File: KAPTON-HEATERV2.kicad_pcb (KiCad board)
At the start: 2 copper layers, 90 x 90 mm, 32 parts, among them J1 XT60PW-M, J2 XT60PW-M, J3 1985276, J4 1985218, J5 10090926-P154XLF, K1 1-1393210-8, Q1 AO3400A, U1 TC4427ACOA, U2 INA181

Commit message: iteration 1.2
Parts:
- removed the R5 at (95.4, 57.0)
- added D3: SMCJ30CA, PCM_JLCPCB:D_SMC, F.Cu at (105.0, 127.5)
- added R8: R27, Resistor_SMD:R_1206_3216Metric, F.Cu at (99.2, 121.2)
- C4: value C19nf -> C4.7nf
- MOSFET1: value SIR462DP-T1-GE3 -> SIR626ADP
- R6: value R10 -> R5
- moved C1 103.9 mm to (58.1, 81.1), turned to 180 degrees
- moved C3 90.3 mm to (76.0, 115.6)
- moved C5 89.2 mm to (76.0, 117.8)
- moved R1 67.4 mm to (62.4, 92.6), turned to 0 degrees
- moved C4 62.6 mm to (99.2, 125.6)
- moved R2 61.8 mm to (63.7, 85.8)
- moved C6 59.8 mm to (72.4, 106.2), turned to 180 degrees
- moved R6 58.4 mm to (53.1, 86.6)
- moved U1 57.7 mm to (58.1, 85.1)
- moved MOSFET1 56.4 mm to (115.0, 128.1)
- moved J4 53.0 mm to (81.0, 66.3), turned to 180 degrees
- moved C2 49.9 mm to (58.1, 78.7), turned to 180 degrees
- moved J5 46.2 mm to (107.7, 70.5), turned to 180 degrees
- moved R3 38.9 mm to (61.8, 81.0)
- moved D1 33.9 mm to (76.0, 96.0), turned to -90 degrees
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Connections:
- net /24VIN renamed Net-(J2-Pin_2)
- D2 pad 3: (no net) -> /24V
- F1 pad 2: unconnected-(F1-Pad2) -> Net-(F1-Pad2)
- J1 pad S1: (no net) -> GND
- J1 pad S2: (no net) -> GND
- K1 pad 3: unconnected-(K1-Pad3) -> Net-(F1-Pad2)
- MOSFET1 pad 4: Net-(C4-Pad1) -> Net-(MOSFET1-Pad4)
- R6 pad 1: Net-(C4-Pad1) -> Net-(MOSFET1-Pad4)
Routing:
- net Current Vout: track 0.00 -> 117.8 mm
- net Net-(MOSFET1-Pad4): track 0.00 -> 110.8 mm
- net HEATER OUT: track 0.00 -> 87.3 mm
- net GND: track 15.8 -> 84.6 mm, vias 2 -> 0
- net TH8: track 94.5 -> 34.6 mm, vias 4 -> 0
- net TH9: track 87.7 -> 32.7 mm, vias 4 -> 0
- net Net-(Q1-Pad1): track 60.5 -> 6.11 mm, vias 4 -> 0
- net TH1: track 95.2 -> 48.9 mm, vias 1 -> 0
- net TH2: track 92.6 -> 47.9 mm, vias 1 -> 0
- net TH5: track 74.9 -> 35.0 mm, vias 3 -> 0
- net TH7: track 79.0 -> 40.6 mm, vias 2 -> 0
- net TH4: track 82.0 -> 45.5 mm, vias 1 -> 0
- net TH3: track 82.6 -> 46.7 mm, vias 1 -> 0
- net PWM: track 7.70 -> 39.2 mm
- net Net-(D1-A): track 48.7 -> 24.2 mm, vias 2 -> 1
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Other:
- board size 90 x 90 mm -> 90 x 76 mm
- board text added: "BRANDON M ASLAN L ZHIHAN C HEATER CONTROL QRET 2025"
- board text added: "IOUT"
- board text added: "PWM"
- board text added: "RELAY"
- board text removed: "BRANDON M ASLAN L QRET 2025"
- board text removed: "PWM IN (3.3V)"
- board text removed: "RELAY (3.3V)"

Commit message: trace fix
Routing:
- net /24V: track 53.0 -> 58.1 mm
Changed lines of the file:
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@@
+	)
+	(segment
+		(start 82.35 117.46)
+		(end 82.35 122.54)
+		(width 4)
+		(layer "F.Cu")
+		(net 18)
 	)
 	(segment
@@
 	)
 	(segment
-		(start 75 130)
+		(start 112.7 131)
+		(end 112.8 130.9)
+		(width 4)
+		(layer "F.Cu")
+		(net 20)
+	)
+	(segment
+		(start 71.4 114.975)
 		(end 71.4 126.4)
+		(width 4)
+		(layer "F.Cu")
+		(net 20)
+	)
+	(segment
+		(start 71.4 126.4)
+		(end 76 131)
 		(width 4)
 		(layer "F.Cu")
@@
 	)
 	(segment
+		(start 76 131)
+		(end 104.9 131)
+		(width 4)
+		(layer "F.Cu")
+		(net 20)
+	)
+	(segment
 		(start 91.5 128.5)
 		(end 90 130)
@@
 	)
 	(segment
+		(start 105 130.9)
+		(end 105.1 131)
+		(width 4)
+		(layer "F.Cu")
+		(net 20)
+	)
+	(segment
 		(start 116.805 130.9)
 		(end 116.905 131)
@@
 	)
 	(segment
-		(start 90 130)
-		(end 75 130)
-		(width 4)
-		(layer "F.Cu")
-		(net 20)
-	)
-	(segment
 		(start 112.8 130.9)
 		(end 116.805 130.9)
@@
 	)
 	(segment
-		(start 90 130)
-		(end 90.9 130.9)
+		(start 105.1 131)
+		(end 112.7 131)
 		(width 4)
 		(layer "F.Cu")
@@
 	)
 	(segment
-		(start 71.4 126.4)
-		(end 71.4 114.975)
-		(width 4)
-		(layer "F.Cu")
-		(net 20)
-	)
-	(segment
 		(start 114.998 128.702)
 		(end 112.8 130.9)
@@
 	)
 	(segment
+		(start 104.9 131)
+		(end 105 130.9)
+		(width 4)
+		(layer "F.Cu")
+		(net 20)
+	)
+	(segment
 		(start 91.7625 119.7375)
 		(end 91.5 120)
@@
 	)
 	(segment
-		(start 90.9 130.9)
-		(end 105 130.9)
-		(width 4)
-		(layer "F.Cu")
-		(net 20)
-	)
-	(segment
 		(start 114.998 129.093)
 		(end 116.905 131)
@@
 		(start 91.5 120)
 		(end 91.5 128.5)
-		(width 4)
-		(layer "F.Cu")
-		(net 20)
-	)
-	(segment
-		(start 105 130.9)
-		(end 112.8 130.9)
 		(width 4)
 		(layer "F.Cu")
@@
 		(min_thickness 0.25)
 		(filled_areas_thickness no)
-		(fill
+		(fill yes
 			(thermal_gap 0.5)
 			(thermal_bridge_width 0.5)

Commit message: fixed DRC issues and made some traces pretty
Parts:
- turned C4 to -90 degrees
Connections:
- J2 pad S1: (no net) -> GND
- J2 pad S2: (no net) -> GND
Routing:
- net GND: track 84.6 -> 112.4 mm
- net TH9: track 32.7 -> 52.3 mm
- net TH4: track 45.5 -> 40.1 mm
- net TH1: track 48.9 -> 53.1 mm
- net TH6: track 98.3 -> 94.9 mm
- net Current Vout: track 117.8 -> 119.7 mm
- net TH7: track 40.6 -> 38.9 mm
- net TH8: track 34.6 -> 35.2 mm
- net TH3: track 46.7 -> 47.3 mm
- net TH2: track 47.9 -> 48.4 mm

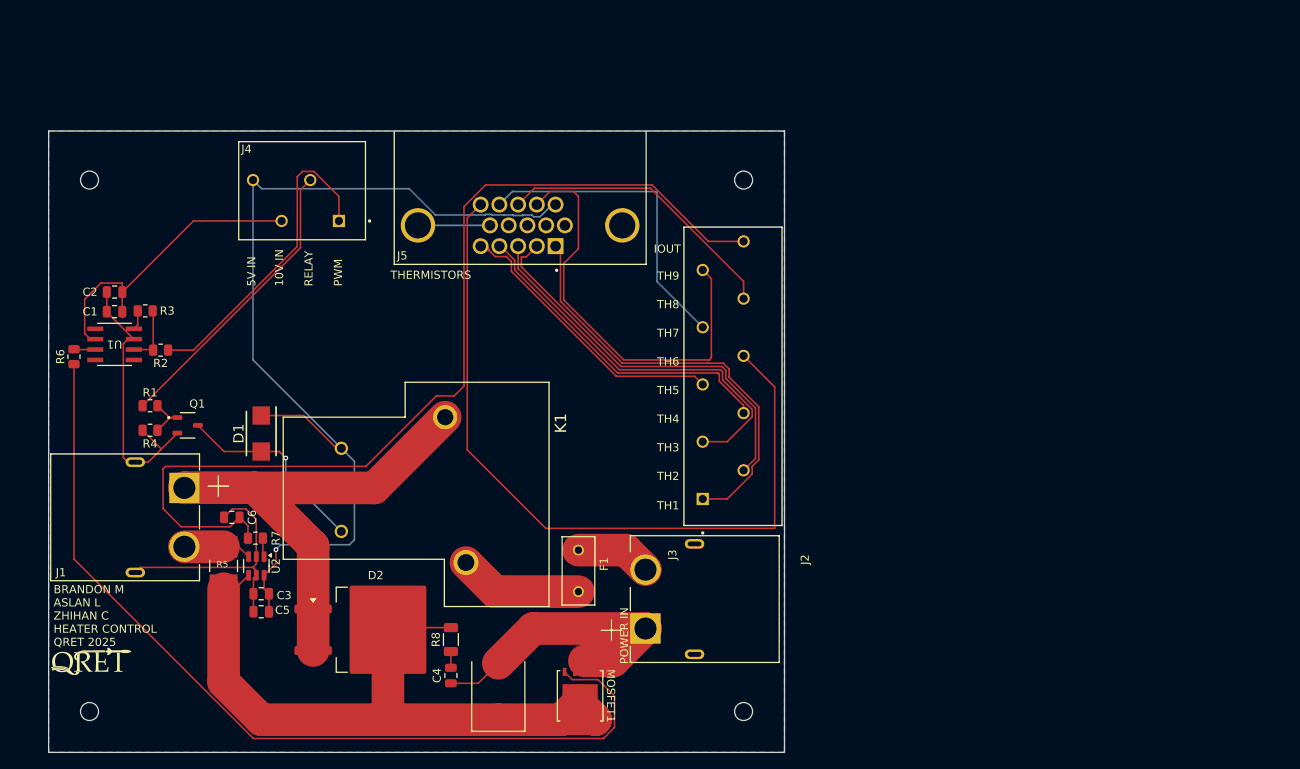
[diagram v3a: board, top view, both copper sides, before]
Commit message: copper pour both sides
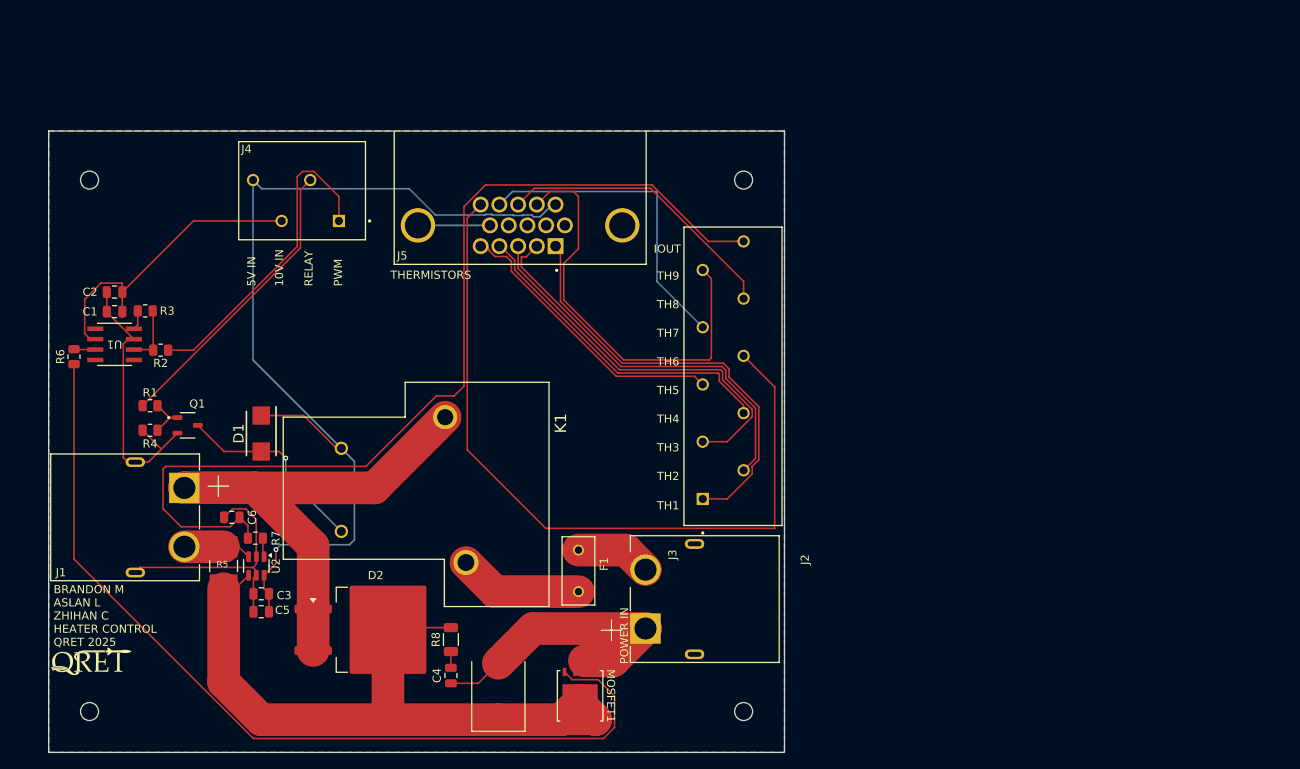
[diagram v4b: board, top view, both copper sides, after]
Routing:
- added copper zone on F.Cu, net GND
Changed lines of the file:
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@@
 		(net 1)
 		(net_name "GND")
-		(layer "B.Cu")
+		(layers "F.Cu" "B.Cu")
 		(hatch edge 0.5)
 		(connect_pads
@@
 		(min_thickness 0.25)
 		(filled_areas_thickness no)
-		(fill yes
+		(fill
 			(thermal_gap 0.5)
 			(thermal_bridge_width 0.5)

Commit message: June 26 New Traces
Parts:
- added C10: C4.7uf, Capacitor_SMD:C_0805_2012Metric, F.Cu at (140.9, 115.7)
- added C7: C4.7uf, Capacitor_SMD:C_0805_2012Metric, F.Cu at (179.5, 111.2)
- added C8: C0.1uf, Capacitor_SMD:C_0805_2012Metric, F.Cu at (182.5, 111.2)
- added C9: C0.1uf, Capacitor_SMD:C_0805_2012Metric, F.Cu at (134.5, 115.7)
- C4: footprint Capacitor_SMD:C_0805_2012Metric -> KCM55LR71J475KH01K:CAPC6153X300N
- D2: value V20DM100C-M3/I -> V20DM100C-M3_I; footprint Package_TO_SOT_SMD:TO-263-2 -> LIB_V20DM100C-M3_I:V40DL45BPM3I
- moved G*** 130.4 mm to (185.5, 129.5)
- moved C1 117.3 mm to (169.5, 117.5), turned to -90 degrees
- moved R6 117.1 mm to (169.4, 100.2), turned to -90 degrees
- moved C2 114.8 mm to (166.1, 117.5), turned to -90 degrees
- moved U1 106.8 mm to (160.3, 115.9), turned to 0 degrees
- moved R3 96.7 mm to (153.0, 113.2)
- moved J4 94.4 mm to (154.9, 125.0), turned to 0 degrees
- moved R2 94.2 mm to (153.0, 115.7), turned to 0 degrees
- moved C6 91.6 mm to (158.9, 75.9), turned to 90 degrees
- moved J5 87.8 mm to (189.0, 103.8), turned to 90 degrees
- moved R7 85.8 mm to (155.0, 76.9), turned to 180 degrees
- moved C5 84.9 mm to (153.4, 82.9), turned to 180 degrees
- moved C3 82.9 mm to (153.4, 85.9), turned to 180 degrees
- moved R1 82.8 mm to (138.0, 126.2), turned to 180 degrees
- moved U2 81.9 mm to (150.4, 79.2)
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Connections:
- D2 pad 1: /24V -> HEATER OUT
- J1 pad S1: GND -> (no net)
- J1 pad S2: GND -> (no net)
- J2 pad S1: GND -> (no net)
- J2 pad S2: GND -> (no net)
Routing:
- net Current Vout: track 119.7 -> 10.6 mm
- net Net-(MOSFET1-Pad4): track 110.8 -> 16.6 mm
- net HEATER OUT: track 87.0 -> 5.05 mm
- net TH6: track 94.9 -> 25.1 mm
- net GND: track 112.4 -> 46.9 mm, vias 0 -> 22
- net /24V: track 58.1 -> 0.00 mm
- net 5V: track 118.7 -> 169.9 mm, vias 1 -> 0
- net PWM: track 39.2 -> 6.27 mm
- net 10V: track 39.2 -> 14.7 mm
- net RELAY: track 36.1 -> 15.0 mm
- net TH1: track 53.1 -> 73.9 mm
- net TH5: track 35.0 -> 15.8 mm
- net Net-(D1-A): track 24.2 -> 41.5 mm, vias 1 -> 0
- net Net-(F1-Pad2): track 15.2 -> 0.00 mm
- net 10V PWM: track 2.56 -> 17.4 mm
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- added copper zone on F.Cu, net /24V
- added copper zone on F.Cu, net HEATER OUT
- added copper zone on F.Cu, net Net-(C4-Pad1)
- added copper zone on F.Cu, net Net-(F1-Pad2)
- added copper zone on F.Cu, net Net-(J2--)
- added copper zone on F.Cu, net SHUNT HIGH
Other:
- board size 90 x 76 mm -> 107 x 63.1 mm
- board text added: "C0.1uf"
- board text added: "C4.7uf"
- board text added: "D3"
- board text added: "R5"
- board text removed: "THERMISTORS"
